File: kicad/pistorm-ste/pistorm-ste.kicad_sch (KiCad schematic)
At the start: 27 parts, among them J1 Raspberry_Pi_2_3, U1 SN54CBTD3384, U2 SN74LVC16373, U3 SN74LVC16373, U4 EPM240T100, U5 SN74LVC16373, U6 SN74LVC16373, U7 SN54CBTD3384, U8 LM1117-3.3

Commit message: Most major connections done. South-side CPLD to work on next
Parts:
- added J2: Conn_01x02_Male, Connector_PinHeader_2.54mm:PinHeader_1x02_P2.54mm_Horizontal, symbol Connector:Conn_01x02_Male
- added JP1: SolderJumper_2_Bridged, Jumper:SolderJumper-2_P1.3mm_Bridged_Pad1.0x1.5mm, symbol Jumper:SolderJumper_2_Bridged
- added R1: 0-100R, Resistor_SMD:R_0805_2012Metric, symbol Device:R
- J_EAST1, J_NORTH1, J_SOUTH1, J_WEST1: value (none) -> Conn_01x17_Male; footprint (none) -> Connector_PinHeader_1.27mm:PinHeader_1x17_P1.27mm_Vertical
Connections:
- net +5V: now also J2.1 (Pin_1), JP1.1 (A); no longer J1.2 (5V), J1.4 (5V)
- net CLK: now also R1.2; no longer J_WEST1.6 (Pin_6)
- net GND: now also J2.2 (Pin_2)
- new net +5V_PI: J1.2 (5V), J1.4 (5V), JP1.2 (B)
- new net CLK_STE: J_WEST1.6 (Pin_6), R1.1
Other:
- note added: "OPTIONAL Auxillery +5V input"

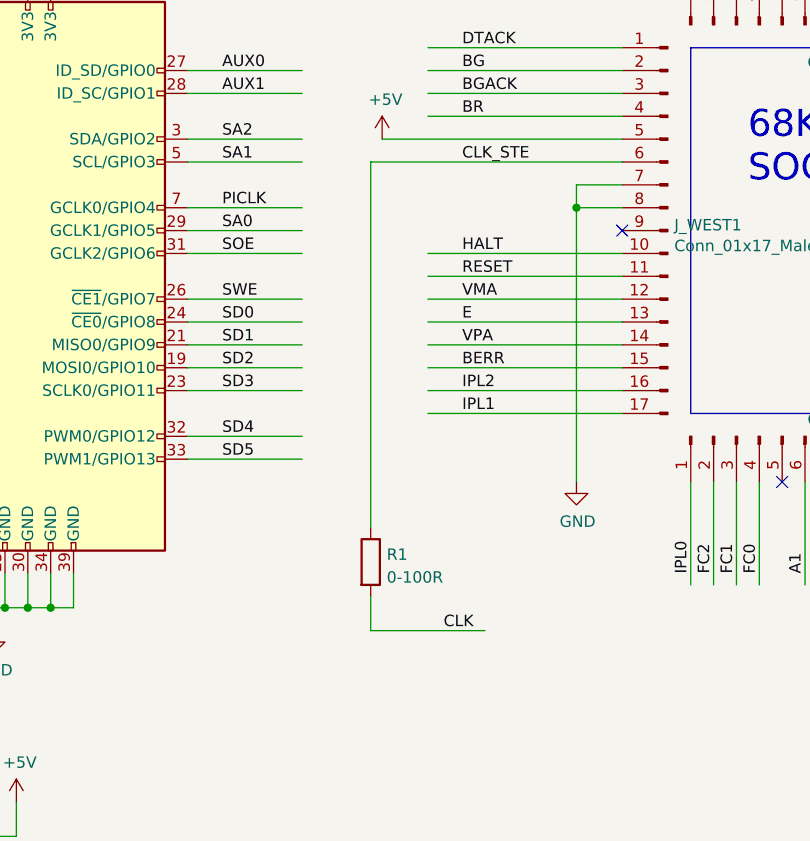
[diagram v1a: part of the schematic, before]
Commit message: Primary routeing completed. Many DRC errors.
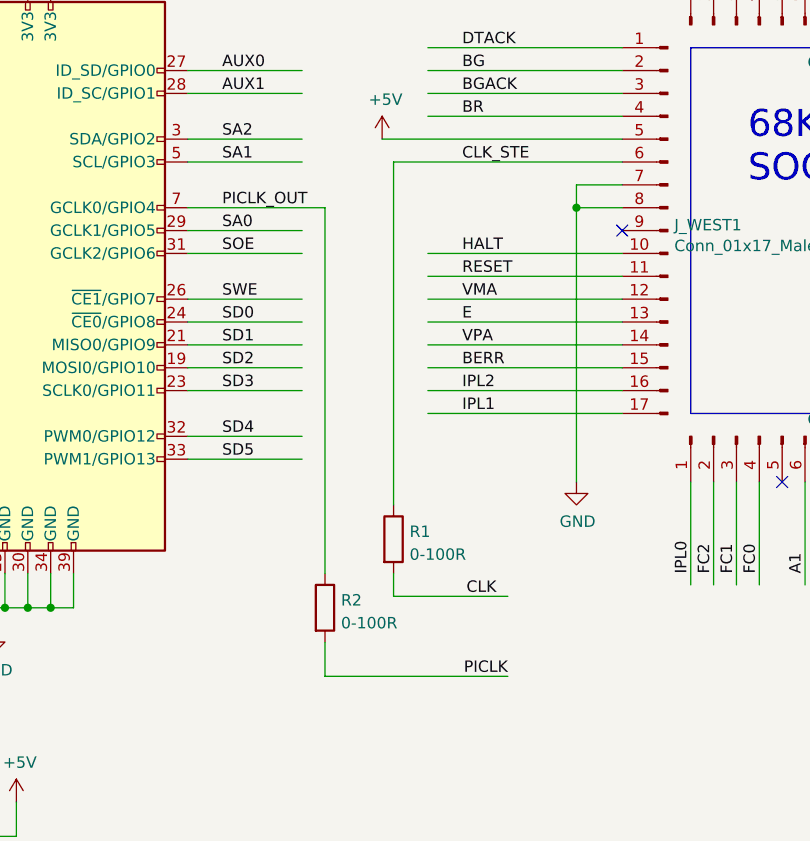
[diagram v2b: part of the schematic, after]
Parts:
- added R2: 0-100R, Resistor_SMD:R_0805_2012Metric, symbol Device:R
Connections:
- net PICLK: now also R2.2; no longer J1.7 (GCLK0/GPIO4)
- new net PICLK_OUT: J1.7 (GCLK0/GPIO4), R2.1
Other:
- moved on the sheet: R1
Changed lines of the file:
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@@
     (stroke (width 0) (type default) (color 0 0 0 0))
   )
-  (wire (pts (xy 96.52 114.3) (xy 109.22 114.3))
+  (wire (pts (xy 99.06 110.49) (xy 111.76 110.49))
     (stroke (width 0) (type default) (color 0 0 0 0))
   )
@@
     (stroke (width 0) (type default) (color 0 0 0 0))
   )
-  (wire (pts (xy 76.2 67.31) (xy 88.9 67.31))
+  (wire (pts (xy 76.2 67.31) (xy 91.44 67.31))
     (stroke (width 0) (type default) (color 0 0 0 0))
   )
@@
     (stroke (width 0) (type default) (color 0 0 0 0))
   )
-  (wire (pts (xy 96.52 62.23) (xy 124.46 62.23))
+  (wire (pts (xy 99.06 62.23) (xy 124.46 62.23))
     (stroke (width 0) (type default) (color 0 0 0 0))
   )
@@
     (stroke (width 0) (type default) (color 0 0 0 0))
   )
+  (wire (pts (xy 91.44 115.57) (xy 91.44 119.38))
+    (stroke (width 0) (type default) (color 0 0 0 0))
+  )
   (wire (pts (xy 193.04 52.07) (xy 180.34 52.07))
     (stroke (width 0) (type default) (color 0 0 0 0))
@@
     (stroke (width 0) (type default) (color 0 0 0 0))
   )
+  (wire (pts (xy 91.44 67.31) (xy 91.44 107.95))
+    (stroke (width 0) (type default) (color 0 0 0 0))
+  )
   (wire (pts (xy 54.61 114.3) (xy 54.61 111.76))
     (stroke (width 0) (type default) (color 0 0 0 0))
   )
+  (wire (pts (xy 91.44 119.38) (xy 111.76 119.38))
+    (stroke (width 0) (type default) (color 0 0 0 0))
+  )
   (wire (pts (xy 25.4 196.85) (xy 38.1 196.85))
     (stroke (width 0) (type default) (color 0 0 0 0))
@@
     (stroke (width 0) (type default) (color 0 0 0 0))
   )
-  (wire (pts (xy 96.52 110.49) (xy 96.52 114.3))
+  (wire (pts (xy 99.06 107.95) (xy 99.06 110.49))
     (stroke (width 0) (type default) (color 0 0 0 0))
   )
@@
     (stroke (width 0) (type default) (color 0 0 0 0))
   )
-  (wire (pts (xy 96.52 62.23) (xy 96.52 102.87))
+  (wire (pts (xy 99.06 62.23) (xy 99.06 100.33))
     (stroke (width 0) (type default) (color 0 0 0 0))
   )
@@
     (effects (font (size 1.27 1.27)) (justify left bottom))
   )
-  (label "CLK" (at 107.95 114.3 180)
+  (label "CLK" (at 110.49 110.49 180)
     (effects (font (size 1.27 1.27)) (justify right bottom))
   )
@@
     (effects (font (size 1.27 1.27)) (justify right bottom))
   )
-  (label "PICLK" (at 80.01 67.31 0)
+  (label "PICLK_OUT" (at 80.01 67.31 0)
     (effects (font (size 1.27 1.27)) (justify left bottom))
   )
@@
     (effects (font (size 1.27 1.27)) (justify right bottom))
   )
+  (label "PICLK" (at 111.76 119.38 180)
+    (effects (font (size 1.27 1.27)) (justify right bottom))
+  )
   (label "SD11" (at 62.23 214.63 0)
     (effects (font (size 1.27 1.27)) (justify left bottom))
@@
     (pin "1")
   )
-  (symbol (lib_id "Device:R") (at 96.52 106.68 0) (unit 1)
+  (symbol (lib_id "Device:R") (at 91.44 111.76 0) (unit 1)
     (in_bom yes) (on_board yes) (fields_autoplaced)
-    (property "Reference" "R1" (id 0) (at 98.298 105.8453 0)
+    (property "Reference" "R2" (id 0) (at 93.218 110.9253 0)
       (effects (font (size 1.27 1.27)) (justify left))
     )
-    (property "Value" "0-100R" (id 1) (at 98.298 108.3822 0)
+    (property "Value" "0-100R" (id 1) (at 93.218 113.4622 0)
       (effects (font (size 1.27 1.27)) (justify left))
     )
-    (property "Footprint" "Resistor_SMD:R_0805_2012Metric" (id 2) (at 94.742 106.68 90)
+    (property "Footprint" "Resistor_SMD:R_0805_2012Metric" (id 2) (at 89.662 111.76 90)
       (effects (font (size 1.27 1.27)) hide)
     )
-    (property "Datasheet" "~" (id 3) (at 96.52 106.68 0)
+    (property "Datasheet" "~" (id 3) (at 91.44 111.76 0)
+      (effects (font (size 1.27 1.27)) hide)
+    )
+    (pin "1")
+    (pin "2")
+  )
+  (symbol (lib_id "Device:R") (at 99.06 104.14 0) (unit 1)
+    (in_bom yes) (on_board yes) (fields_autoplaced)
+    (property "Reference" "R1" (id 0) (at 100.838 103.3053 0)
+      (effects (font (size 1.27 1.27)) (justify left))
+    )
+    (property "Value" "0-100R" (id 1) (at 100.838 105.8422 0)
+      (effects (font (size 1.27 1.27)) (justify left))
+    )
+    (property "Footprint" "Resistor_SMD:R_0805_2012Metric" (id 2) (at 97.282 104.14 90)
+      (effects (font (size 1.27 1.27)) hide)
+    )
+    (property "Datasheet" "~" (id 3) (at 99.06 104.14 0)
       (effects (font (size 1.27 1.27)) hide)
     )
@@
       (reference "R1") (unit 1) (value "0-100R") (footprint "Resistor_SMD:R_0805_2012Metric")
     )
+    (path "/2504d6d9-c58a-484b-bfac-07587eb7cb2c"
+      (reference "R2") (unit 1) (value "0-100R") (footprint "Resistor_SMD:R_0805_2012Metric")
+    )
     (path "/00000000-0000-0000-0000-000064f6c161"

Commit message: Routing complete and passing DRC. Query PLCC socket alignment. Will change to a single footprint.
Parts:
- added R1, R2: 4k7, Resistor_SMD:R_0805_2012Metric, symbol Device:R
- renumbered R1 to R3, R2 to R4
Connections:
- net +3V3: now also R1.1, R2.1
- net TDI: now also R1.2
- net TMS: now also R2.2
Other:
- note added: "CONSIDER PULL UPS?"
- note removed: "CHECK LATCHES RUN FROM 3V3 CONSIDER PULL UPS?"
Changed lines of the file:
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@@
   (junction (at 214.63 236.22) (diameter 0) (color 0 0 0 0)
   )
+  (junction (at 295.91 130.81) (diameter 0) (color 0 0 0 0)
+  )
   (junction (at 74.93 248.92) (diameter 0) (color 0 0 0 0)
   )
@@
     (stroke (width 0) (type default) (color 0 0 0 0))
   )
+  (wire (pts (xy 295.91 130.81) (xy 304.8 130.81))
+    (stroke (width 0) (type default) (color 0 0 0 0))
+  )
   (wire (pts (xy 152.4 109.22) (xy 152.4 97.79))
     (stroke (width 0) (type default) (color 0 0 0 0))
@@
     (stroke (width 0) (type default) (color 0 0 0 0))
   )
+  (wire (pts (xy 295.91 138.43) (xy 295.91 143.51))
+    (stroke (width 0) (type default) (color 0 0 0 0))
+  )
   (wire (pts (xy 361.95 29.21) (xy 359.41 29.21))
     (stroke (width 0) (type default) (color 0 0 0 0))
@@
     (stroke (width 0) (type default) (color 0 0 0 0))
   )
+  (wire (pts (xy 381 19.05) (xy 381 22.86))
+    (stroke (width 0) (type default) (color 0 0 0 0))
+  )
   (wire (pts (xy 48.26 111.76) (xy 50.8 111.76))
     (stroke (width 0) (type default) (color 0 0 0 0))
@@
     (stroke (width 0) (type default) (color 0 0 0 0))
   )
-  (wire (pts (xy 328.93 140.97) (xy 341.63 140.97))
+  (wire (pts (xy 304.8 140.97) (xy 341.63 140.97))
     (stroke (width 0) (type default) (color 0 0 0 0))
   )
@@
     (stroke (width 0) (type default) (color 0 0 0 0))
   )
+  (wire (pts (xy 304.8 138.43) (xy 304.8 140.97))
+    (stroke (width 0) (type default) (color 0 0 0 0))
+  )
   (wire (pts (xy 123.19 254) (xy 139.7 254))
     (stroke (width 0) (type default) (color 0 0 0 0))
@@
     (stroke (width 0) (type default) (color 0 0 0 0))
   )
+  (wire (pts (xy 295.91 127) (xy 295.91 130.81))
+    (stroke (width 0) (type default) (color 0 0 0 0))
+  )
   (wire (pts (xy 276.86 176.53) (xy 260.35 176.53))
     (stroke (width 0) (type default) (color 0 0 0 0))
@@
     (stroke (width 0) (type default) (color 0 0 0 0))
   )
-  (wire (pts (xy 328.93 143.51) (xy 341.63 143.51))
+  (wire (pts (xy 295.91 143.51) (xy 341.63 143.51))
     (stroke (width 0) (type default) (color 0 0 0 0))
   )
@@
     (stroke (width 0) (type default) (color 0 0 0 0))
   )
+  (wire (pts (xy 381 22.86) (xy 370.84 22.86))
+    (stroke (width 0) (type default) (color 0 0 0 0))
+  )
   (wire (pts (xy 250.19 124.46) (xy 270.51 124.46))
     (stroke (width 0) (type default) (color 0 0 0 0))
@@
     (effects (font (size 2.9972 2.9972)) (justify left bottom))
   )
-  (text "CHECK LATCHES RUN FROM 3V3\nCONSIDER PULL UPS?" (at 17.78 278.13 0)
+  (text "CONSIDER PULL UPS?" (at 17.78 278.13 0)
     (effects (font (size 5.0038 5.0038)) (justify left bottom))
   )
@@
     (effects (font (size 1.27 1.27)) (justify right bottom))
   )
+  (label "+5V_PI" (at 372.11 22.86 0)
+    (effects (font (size 1.27 1.27)) (justify left bottom))
+  )
   (label "D7" (at 26.67 201.93 0)
     (effects (font (size 1.27 1.27)) (justify left bottom))
@@
     (pin "1")
   )
+  (symbol (lib_id "Device:R") (at 304.8 134.62 0) (unit 1)
+    (in_bom yes) (on_board yes) (fields_autoplaced)
+    (property "Reference" "R2" (id 0) (at 306.578 133.7853 0)
+      (effects (font (size 1.27 1.27)) (justify left))
+    )
+    (property "Value" "4k7" (id 1) (at 306.578 136.3222 0)
+      (effects (font (size 1.27 1.27)) (justify left))
+    )
+    (property "Footprint" "Resistor_SMD:R_0805_2012Metric" (id 2) (at 303.022 134.62 90)
+      (effects (font (size 1.27 1.27)) hide)
+    )
+    (property "Datasheet" "~" (id 3) (at 304.8 134.62 0)
+      (effects (font (size 1.27 1.27)) hide)
+    )
+    (pin "1")
+    (pin "2")
+  )
   (symbol (lib_id "Device:R") (at 91.44 111.76 0) (unit 1)
     (in_bom yes) (on_board yes) (fields_autoplaced)
-    (property "Reference" "R2" (id 0) (at 93.218 110.9253 0)
+    (property "Reference" "R4" (id 0) (at 93.218 110.9253 0)
       (effects (font (size 1.27 1.27)) (justify left))
     )
@@
     (pin "2")
   )
+  (symbol (lib_id "Device:R") (at 295.91 134.62 0) (unit 1)
+    (in_bom yes) (on_board yes) (fields_autoplaced)
+    (property "Reference" "R1" (id 0) (at 297.688 133.7853 0)
+      (effects (font (size 1.27 1.27)) (justify left))
+    )
+    (property "Value" "4k7" (id 1) (at 297.688 136.3222 0)
+      (effects (font (size 1.27 1.27)) (justify left))
+    )
+    (property "Footprint" "Resistor_SMD:R_0805_2012Metric" (id 2) (at 294.132 134.62 90)
+      (effects (font (size 1.27 1.27)) hide)
+    )
+    (property "Datasheet" "~" (id 3) (at 295.91 134.62 0)
+      (effects (font (size 1.27 1.27)) hide)
+    )
+    (pin "1")
+    (pin "2")
+  )
   (symbol (lib_id "Device:R") (at 99.06 104.14 0) (unit 1)
     (in_bom yes) (on_board yes) (fields_autoplaced)
-    (property "Reference" "R1" (id 0) (at 100.838 103.3053 0)
+    (property "Reference" "R3" (id 0) (at 100.838 103.3053 0)
       (effects (font (size 1.27 1.27)) (justify left))
     )
@@
     (pin "2")
   )
+  (symbol (lib_id "power:+3V3") (at 295.91 127 0) (unit 1)
+    (in_bom yes) (on_board yes)
+    (property "Reference" "#PWR0129" (id 0) (at 295.91 130.81 0)
+      (effects (font (size 1.27 1.27)) hide)
+    )
+    (property "Value" "+3V3" (id 1) (at 296.291 122.6058 0))
+    (property "Footprint" "" (id 2) (at 295.91 127 0)
+      (effects (font (size 1.27 1.27)) hide)
+    )
+    (property "Datasheet" "" (id 3) (at 295.91 127 0)
+      (effects (font (size 1.27 1.27)) hide)
+    )
+    (pin "1")
+  )
+  (symbol (lib_id "power:PWR_FLAG") (at 381 19.05 0) (unit 1)
+    (in_bom yes) (on_board yes)
+    (property "Reference" "#FLG0103" (id 0) (at 381 17.145 0)
+      (effects (font (size 1.27 1.27)) hide)
+    )
+    (property "Value" "PWR_FLAG" (id 1) (at 381 14.6558 0))
+    (property "Footprint" "" (id 2) (at 381 19.05 0)
+      (effects (font (size 1.27 1.27)) hide)
+    )
+    (property "Datasheet" "~" (id 3) (at 381 19.05 0)
+      (effects (font (size 1.27 1.27)) hide)
+    )
+    (pin "1")
+  )
   (symbol (lib_id "power:GND") (at 57.15 142.24 0) (unit 1)
     (in_bom yes) (on_board yes)
@@
       (reference "#FLG0102") (unit 1) (value "PWR_FLAG") (footprint "")
     )
+    (path "/bfb5c702-4bcf-4182-bd43-68207304e0b8"
+      (reference "#FLG0103") (unit 1) (value "PWR_FLAG") (footprint "")
+    )
     (path "/f4331473-c3ba-47c7-86ff-e8c464396466"
       (reference "#PWR01") (unit 1) (value "+5V") (footprint "")
@@
       (reference "#PWR0128") (unit 1) (value "GND") (footprint "")
     )
+    (path "/b9cbaca6-976c-4247-a87b-02ac29d22cff"
+      (reference "#PWR0129") (unit 1) (value "+3V3") (footprint "")
+    )
     (path "/00000000-0000-0000-0000-00006589efc0"
       (reference "C1") (unit 1) (value "100n") (footprint "Capacitor_SMD:C_0805_2012Metric")
@@
       (reference "J_WEST1") (unit 1) (value "Conn_01x17_Male") (footprint "Connector_PinHeader_1.27mm:PinHeader_1x17_P1.27mm_Vertical")
     )
+    (path "/6831bbb9-99bf-43e2-9cb2-521d8885d5c0"
+      (reference "R1") (unit 1) (value "4k7") (footprint "Resistor_SMD:R_0805_2012Metric")
+    )
+    (path "/07ad9709-90ab-4d9e-b536-a8c12eae3c59"
+      (reference "R2") (unit 1) (value "4k7") (footprint "Resistor_SMD:R_0805_2012Metric")
+    )
     (path "/80367d4d-6f53-4267-a733-5c028c087845"
-      (reference "R1") (unit 1) (value "0-100R") (footprint "Resistor_SMD:R_0805_2012Metric")
+      (reference "R3") (unit 1) (value "0-100R") (footprint "Resistor_SMD:R_0805_2012Metric")
     )
     (path "/2504d6d9-c58a-484b-bfac-07587eb7cb2c"
-      (reference "R2") (unit 1) (value "0-100R") (footprint "Resistor_SMD:R_0805_2012Metric")
+      (reference "R4") (unit 1) (value "0-100R") (footprint "Resistor_SMD:R_0805_2012Metric")
     )
     (path "/00000000-0000-0000-0000-000064f6c161"

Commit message: Passing DRC. Fixed 3d model issue with the plug footprint.
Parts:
- removed J_EAST1, J_NORTH1, J_SOUTH1, J_WEST1: Conn_01x17_Male, Connector_PinHeader_1.27mm:PinHeader_1x17_P1.27mm_Vertical, symbol Connector:Conn_01x17_Male
- added J2: PLCC68_plug, PLCC_plugs:PLCC68_male_pins, symbol PLCC_plugs:PLCC68_plug
- renumbered J2 to J3
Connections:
- net +5V: now also J2.14 (Pin_14), J2.52 (Pin_52)
- net A1: now also J2.32 (Pin_32)
- net A10: now also J2.41 (Pin_41)
- net A11: now also J2.42 (Pin_42)
- net A12: now also J2.43 (Pin_43)
- net A13: now also J2.44 (Pin_44)
- net A14: now also J2.45 (Pin_45)
- net A15: now also J2.46 (Pin_46)
- net A16: now also J2.47 (Pin_47)
- net A17: now also J2.48 (Pin_48)
- net A18: now also J2.49 (Pin_49)
- net A19: now also J2.50 (Pin_50)
- net A2: now also J2.33 (Pin_33)
- net A20: now also J2.51 (Pin_51)
- net A21: now also J2.53 (Pin_53)
- net A22: now also J2.54 (Pin_54)
- net A23: now also J2.55 (Pin_55)
- net A3: now also J2.34 (Pin_34)
- net A4: now also J2.35 (Pin_35)
- net A5: now also J2.36 (Pin_36)
- net A6: now also J2.37 (Pin_37)
- net A7: now also J2.38 (Pin_38)
- net A8: now also J2.39 (Pin_39)
- net A9: now also J2.40 (Pin_40)
- net AS: now also J2.6 (Pin_6)
- net BERR: now also J2.24 (Pin_24)
- net BG: now also J2.11 (Pin_11)
- net BGACK: now also J2.12 (Pin_12)
- net BR: now also J2.13 (Pin_13)
- net CLK_STE: now also J2.15 (Pin_15)
- net D0: now also J2.5 (Pin_5)
- net D1: now also J2.4 (Pin_4)
- net D10: now also J2.63 (Pin_63)
- net D11: now also J2.62 (Pin_62)
- net D12: now also J2.61 (Pin_61)
- net D13: now also J2.60 (Pin_60)
- net D14: now also J2.59 (Pin_59)
- net D15: now also J2.58 (Pin_58)
- net D2: now also J2.3 (Pin_3)
- net D3: now also J2.2 (Pin_2)
- net D4: now also J2.1 (Pin_1)
- net D5: now also J2.68 (Pin_68)
- net D6: now also J2.67 (Pin_67)
- net D7: now also J2.66 (Pin_66)
- net D8: now also J2.65 (Pin_65)
- net D9: now also J2.64 (Pin_64)
- net DTACK: now also J2.10 (Pin_10)
- net E: now also J2.22 (Pin_22)
- net FC0: now also J2.30 (Pin_30)
- net FC1: now also J2.29 (Pin_29)
- net FC2: now also J2.28 (Pin_28)
- net GND: now also J2.16 (Pin_16), J2.17 (Pin_17), J2.56 (Pin_56), J2.57 (Pin_57)
- net HALT: now also J2.19 (Pin_19)
- net IPL0: now also J2.27 (Pin_27)
- net IPL1: now also J2.26 (Pin_26)
- net IPL2: now also J2.25 (Pin_25)
- net LDS: now also J2.8 (Pin_8)
- net RESET: now also J2.20 (Pin_20)
- net RW: now also J2.9 (Pin_9)
- net UDS: now also J2.7 (Pin_7)
- net VMA: now also J2.21 (Pin_21)
- net VPA: now also J2.23 (Pin_23)
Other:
- moved on the sheet: R3
